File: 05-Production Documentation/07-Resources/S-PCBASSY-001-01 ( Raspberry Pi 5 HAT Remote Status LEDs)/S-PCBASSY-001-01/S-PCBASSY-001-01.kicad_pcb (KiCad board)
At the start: 2 copper layers, 65 x 56 mm, 43 parts, among them J1 GPIO, J2 43650-0428, Q1 BSS138, Q2 BSS138, Q3 BSS138, Q4 AO3401A, U1 CAT24C256

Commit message: Layout done
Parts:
- removed the J1 at (50.1, 50.6)
- moved Rpd1 118.0 mm to (140.9, 72.5), turned to 90 degrees
- moved Rpd2 115.0 mm to (140.8, 65.0), turned to 90 degrees
- moved Rpd3 113.0 mm to (140.8, 58.0), turned to 90 degrees
- moved Rg4 108.2 mm to (148.4, 72.5)
- moved U1 106.1 mm to (131.0, 58.5), turned to 90 degrees
- moved Rg3 104.2 mm to (139.8, 55.5)
- moved Rg6 104.2 mm to (148.3, 65.0)
- moved Rg5 103.1 mm to (148.3, 58.0)
- moved Rg2 100.3 mm to (139.9, 70.0)
- moved Rg1 98.4 mm to (139.8, 62.5)
- moved D7 91.4 mm to (154.7, 68.5), turned to 180 degrees
- moved D8 90.9 mm to (154.7, 65.5), turned to 180 degrees
- moved D9 90.8 mm to (154.7, 62.5), turned to 180 degrees
- moved J2 84.7 mm to (159.5, 71.5), turned to -90 degrees
- moved D6 81.9 mm to (147.3, 56.1), turned to 90 degrees
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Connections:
- C2 pad 1: Net-(D10-K) -> +5V
- C3 pad 1: Net-(D10-K) -> +5V
- D10 pad 1: Net-(D10-K) -> +5V
- D11 pad 1: Net-(D10-K) -> +5V
- F1 pad 1: Net-(D10-K) -> +5V

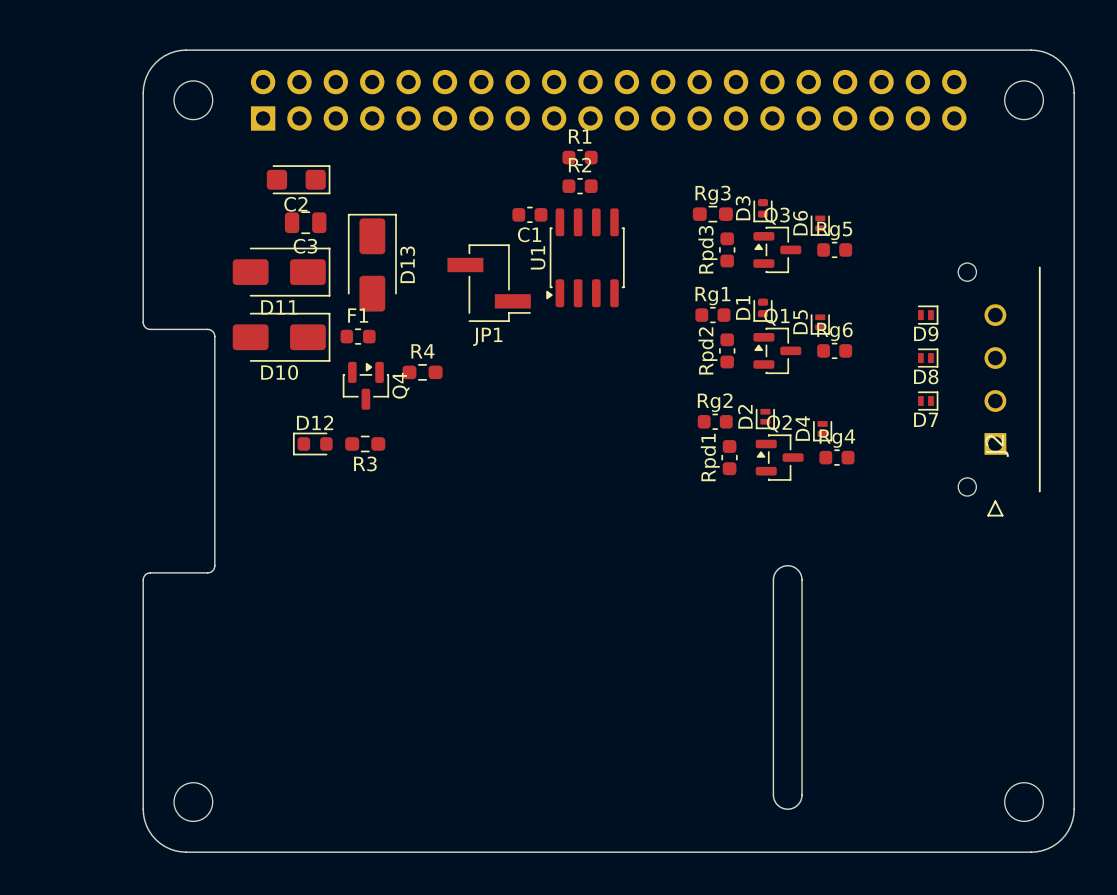
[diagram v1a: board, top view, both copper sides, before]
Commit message: PCB Routing done
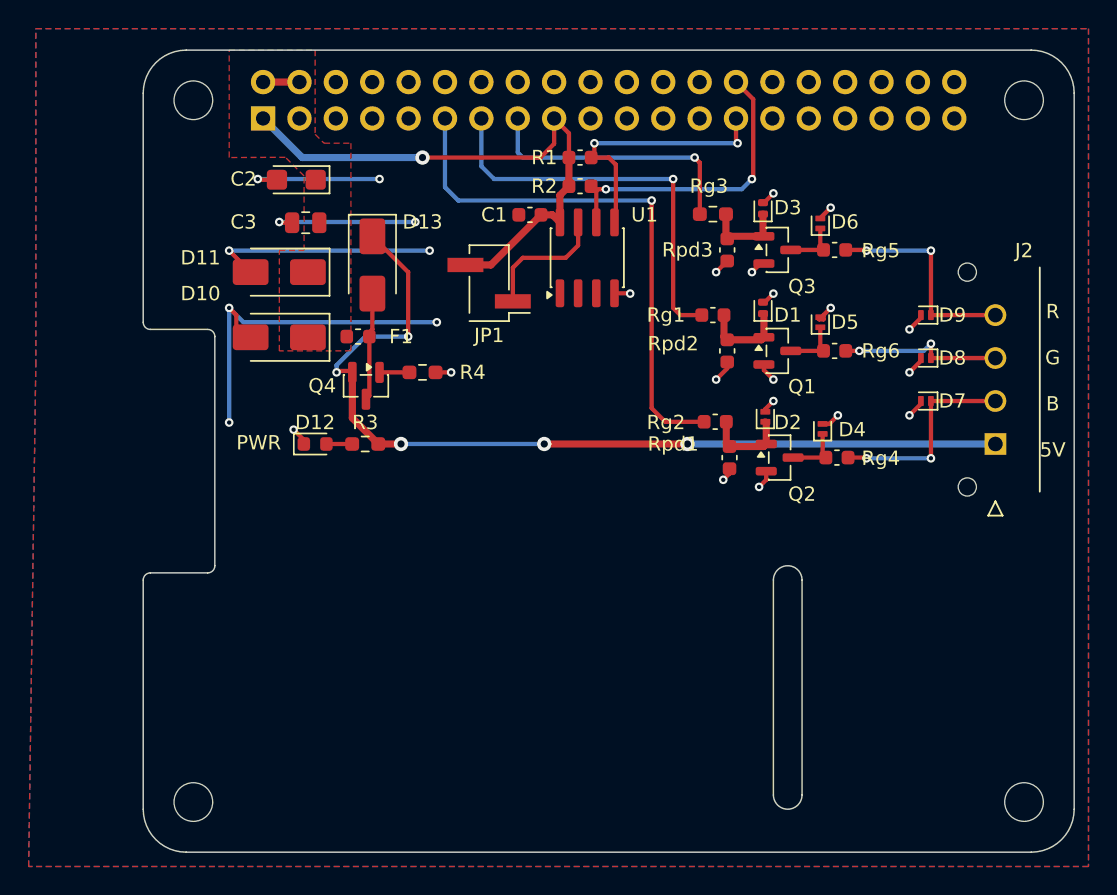
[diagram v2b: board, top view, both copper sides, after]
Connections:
- net /GPIO10/SPI0.MOSI renamed /RPi_Processor_Interface/GPIO10/SPI0.MOSI
- net /GPIO11/SPI0.SCLK renamed /RPi_Processor_Interface/GPIO11/SPI0.SCLK
- net /GPIO12/PWM0 renamed /RPi_Processor_Interface/GPIO12/PWM0
- net /GPIO13/PWM1 renamed /RPi_Processor_Interface/GPIO13/PWM1
- net /GPIO14/TXD0 renamed /RPi_Processor_Interface/GPIO14/TXD0
- net /GPIO15/RXD0 renamed /RPi_Processor_Interface/GPIO15/RXD0
- net /GPIO16 renamed /RPi_Processor_Interface/GPIO16
- net /GPIO18/PCM.CLK renamed /RPi_Processor_Interface/GPIO18/PCM.CLK
- net /GPIO19/PCM.FS renamed /RPi_Processor_Interface/GPIO19/PCM.FS
- net /GPIO20/PCM.DIN renamed /RPi_Processor_Interface/GPIO20/PCM.DIN
- net /GPIO21/PCM.DOUT renamed /RPi_Processor_Interface/GPIO21/PCM.DOUT
- net /GPIO23 renamed /RPi_Processor_Interface/GPIO23
- net /GPIO24 renamed /RPi_Processor_Interface/GPIO24
- net /GPIO25 renamed /RPi_Processor_Interface/GPIO25
- net /GPIO26 renamed /RPi_Processor_Interface/GPIO26
- net /GPIO2/SDA1 renamed /RPi_Processor_Interface/GPIO2/SDA1
- net /GPIO3/SCL1 renamed /RPi_Processor_Interface/GPIO3/SCL1
- net /GPIO4/GPCLK0 renamed /RPi_Processor_Interface/GPIO4/GPCLK0
- net /GPIO5 renamed /RPi_Processor_Interface/GPIO5
- net /GPIO6 renamed /RPi_Processor_Interface/GPIO6
- net /GPIO7/SPI0.CE1 renamed /RPi_Processor_Interface/GPIO7/SPI0.CE1
- net /GPIO8/SPI0.CE0 renamed /RPi_Processor_Interface/GPIO8/SPI0.CE0
- net /GPIO9/SPI0.MISO renamed /RPi_Processor_Interface/GPIO9/SPI0.MISO
- D13 pad 1: +5V -> +5FV
- J1 pad 11: /GPIO17 -> /LED_Driver_Array/POWER_LED_IN
- J1 pad 13: /GPIO27 -> /LED_Driver_Array/MEDIA_LED_IN
- J1 pad 15: /GPIO22 -> /LED_Driver_Array/ERROR_IN
- J1 pad 27: /ID_SDA -> /RPi_Processor_Interface/ID_SDA
- J1 pad 28: /ID_SCL -> /RPi_Processor_Interface/ID_SCL
- J2 pad 1: +5V -> +5FV
- Q4 pad 2: +5V -> +5FV
- R3 pad 1: +5V -> +5FV
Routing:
- net GND: track 0.00 -> 83.8 mm, vias 0 -> 27
- net +5FV: track 0.00 -> 64.4 mm, vias 0 -> 5
- net +3V3: track 0.00 -> 39.8 mm, vias 0 -> 1
- net /LED_Driver_Array/POWER_LED_IN: track 0.00 -> 38.2 mm, vias 0 -> 1
- net /LED_Driver_Array/MEDIA_LED_IN: track 0.00 -> 28.3 mm, vias 0 -> 1
- net /RPi_Processor_Interface/ID_SCL: track 0.00 -> 21.6 mm, vias 0 -> 2
- net /LED_Driver_Array/ERROR_IN: track 0.00 -> 19.0 mm, vias 0 -> 1
- net /RPi_Processor_Interface/ID_SDA: track 0.00 -> 18.9 mm, vias 0 -> 2
- net /External_Connector/CONNECTOR_CATHODE_ERROR: track 0.00 -> 15.0 mm, vias 0 -> 2
- net /External_Connector/CONNECTOR_CATHODE_POWER: track 0.00 -> 14.3 mm, vias 0 -> 2
- net /External_Connector/CONNECTOR_CATHODE_MEDIA: track 0.00 -> 11.7 mm, vias 0 -> 2
- net Net-(JP1-A): track 0.00 -> 9.16 mm
- net Net-(D13-A): track 0.00 -> 7.56 mm
- net Net-(D1-K): track 0.00 -> 6.13 mm
- net Net-(D2-K): track 0.00 -> 6.03 mm
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- added copper zone on F.Cu, net +5V
- added copper zone on B.Cu, net GND
- added copper zone on F.Cu, net GND
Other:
- board text added: "PWR"
- board text added: "R G B 5V"
